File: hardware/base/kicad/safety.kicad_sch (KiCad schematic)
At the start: 14 parts, among them J18 ESTOP, U34 LTV-357T-C, U35 TPS3828-33DBVR

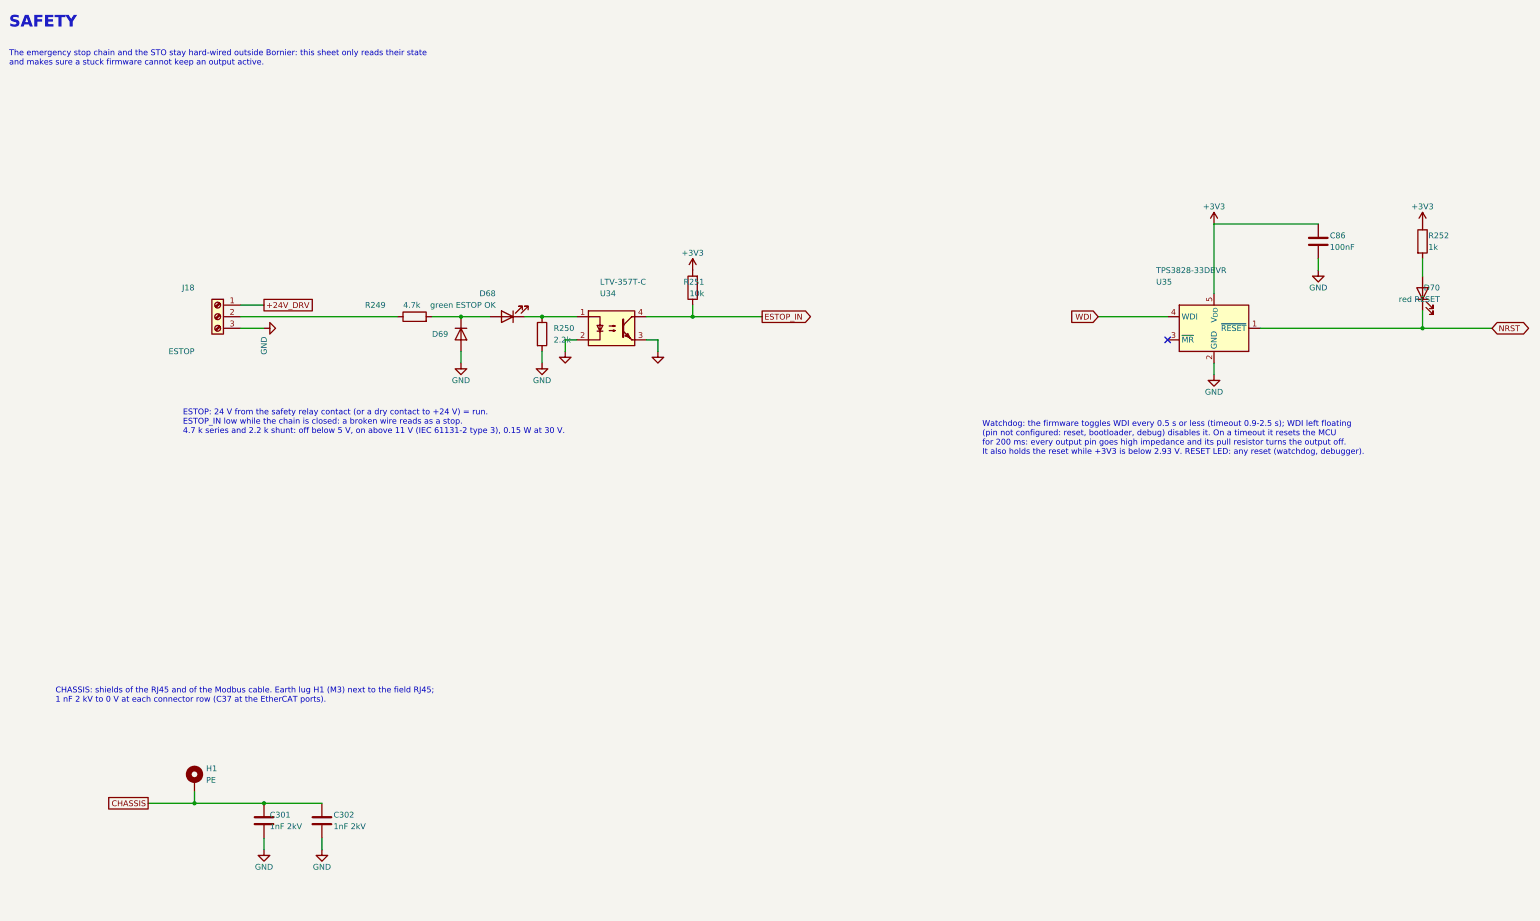
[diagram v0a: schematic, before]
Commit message: Harden the base board protections and unify its terminal blocks
- TVS (SMBJ33CA) on the spindle EN and DIR drains: a relay coil driven
  without a flyback diode no longer avalanches the FET.
- ESD (5 x TPD4E05U06) on every signal of the local bus header.
- A single terminal block type, KF2EDGR-3.81-4P, five times. Pinout rule:
  pole 1 withstands 24 V, pole 2 is 0 V, so the power plug damages
  nothing whichever header it lands in.
- Functional earth on pole 3 of the power terminal block, replacing the
  M3 earth lug.
- 100 k pull-down on the DAC node: the 0-10 V output stays at 0 V while
  the DAC pin is not configured (reset, bootloader).
- "24V OUT" LED on +24V_DRV and test points on the four rails.
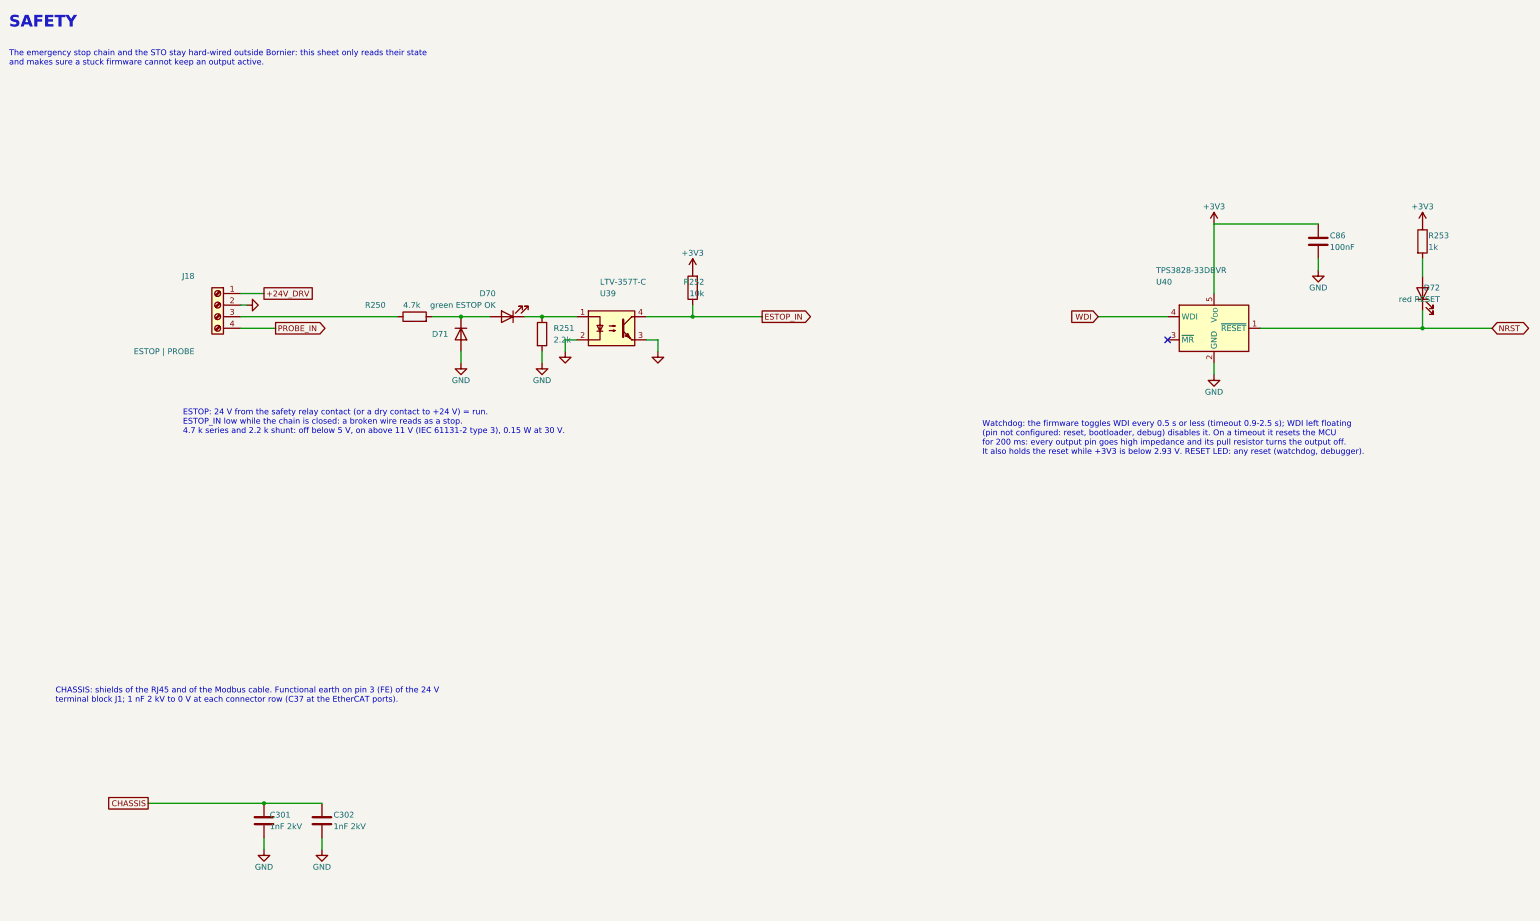
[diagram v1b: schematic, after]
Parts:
- removed D68: green ESTOP OK, LED_SMD:LED_0603_1608Metric, symbol Device:LED
- removed D69: 1N4148WS, Diode_SMD:D_SOD-323, symbol Device:D
- removed H1: PE, MountingHole:MountingHole_3.2mm_M3_Pad_Via, symbol Mechanical:MountingHole_Pad
- removed R249: 4.7k, Resistor_SMD:R_1206_3216Metric, symbol Device:R
- removed U34: LTV-357T-C, Package_SO:SO-4_4.4x3.6mm_P2.54mm, symbol Isolator:LTV-357T
- removed U35: TPS3828-33DBVR, Package_TO_SOT_SMD:SOT-23-5, symbol Power_Supervisor:TPS3823-xxDBV
- added D71: 1N4148WS, Diode_SMD:D_SOD-323, symbol Device:D
- added D72: red RESET, LED_SMD:LED_0603_1608Metric, symbol Device:LED
- added R253: 1k, Resistor_SMD:R_0402_1005Metric, symbol Device:R
- added U39: LTV-357T-C, Package_SO:SO-4_4.4x3.6mm_P2.54mm, symbol Isolator:LTV-357T
- added U40: TPS3828-33DBVR, Package_TO_SOT_SMD:SOT-23-5, symbol Power_Supervisor:TPS3823-xxDBV
- D70: value red RESET -> green ESTOP OK; LCSC C2286 -> C2289
- J18: value ESTOP -> ESTOP | PROBE; footprint Connector_Phoenix_MC:PhoenixContact_MC_1,5_3-G-3.81_1x03_P3.81mm_Horizontal -> Connector_Phoenix_MC:PhoenixContact_MC_1,5_4-G-3.81_1x04_P3.81mm_Horizontal; symbol Connector:Screw_Terminal_01x03 -> Connector:Screw_Terminal_01x04; LCSC C441183 -> C441184
- R250: value 2.2k -> 4.7k; footprint Resistor_SMD:R_0402_1005Metric -> Resistor_SMD:R_1206_3216Metric; LCSC C25879 -> C17936
- R251: value 10k -> 2.2k; LCSC C25744 -> C25879
- R252: value 1k -> 10k; LCSC C11702 -> C25744
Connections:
- net +3V3: now also R252.2, R253.1, U40.5 (V_{DD}); no longer R251.2, R252.1
- net ESTOP_IN: now also R252.1, U39.4; no longer R251.1
- net GND: now also J18.2 (Pin_2), R251.2, D71.2 (A), U39.2, U39.3, U40.2 (GND); no longer J18.3 (Pin_3), R250.2
- net NRST: now also D72.1 (K), U40.1 (~{RESET}); no longer D70.1 (K)
- net WDI: now also U40.4 (WDI)
- net at D70.2 (A): now also R250.2, D71.1 (K); no longer R252.2
- net at R250.1: now also J18.3 (Pin_3)
- new net: D70.1 (K), R251.1, U39.1
- new net: D72.2 (A), R253.2
- new net PROBE_IN: J18.4 (Pin_4)
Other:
- note added: "CHASSIS: shields of the RJ45 and of the Modbus cable. Functional earth on pin 3 (FE) of the 24 V terminal block J1; 1 nF 2 kV to 0 V at each connector row (C37 at the EtherCAT ports)."
- note removed: "CHASSIS: shields of the RJ45 and of the Modbus cable. Earth lug H1 (M3) next to the field RJ45; 1 nF 2 kV to 0 V at each connector row (C37 at the EtherCAT ports)."
- moved on the sheet: D70, R250, R251, R252

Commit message: Accept a 12 V or 24 V supply on the base board (10.8 to 30 V)
- Supply nets renamed +VIN and +VIN_OUT (silkscreen VIN OUT).
- UVLO 200 k over 47 k // 100 k: start 8.47 V (9.48 V worst case),
  stop 7.79 V; fuse 3.5 A (12H1350C).
- 0-10 V: OPA2990 rail-to-rail op amp supplied by +VIN, SS8550 current
  limit across the 120 ohm; 10 V into 10 k from 10.9 V of supply.
- E-stop and probe inputs: 2 x 4.7 k in parallel, shunts 1 k and 4.7 k.
- Buck simulated from 7.8 to 30 V with the smallest slope compensation
  the datasheet allows: 79 deg, 11.6 dB minimum.
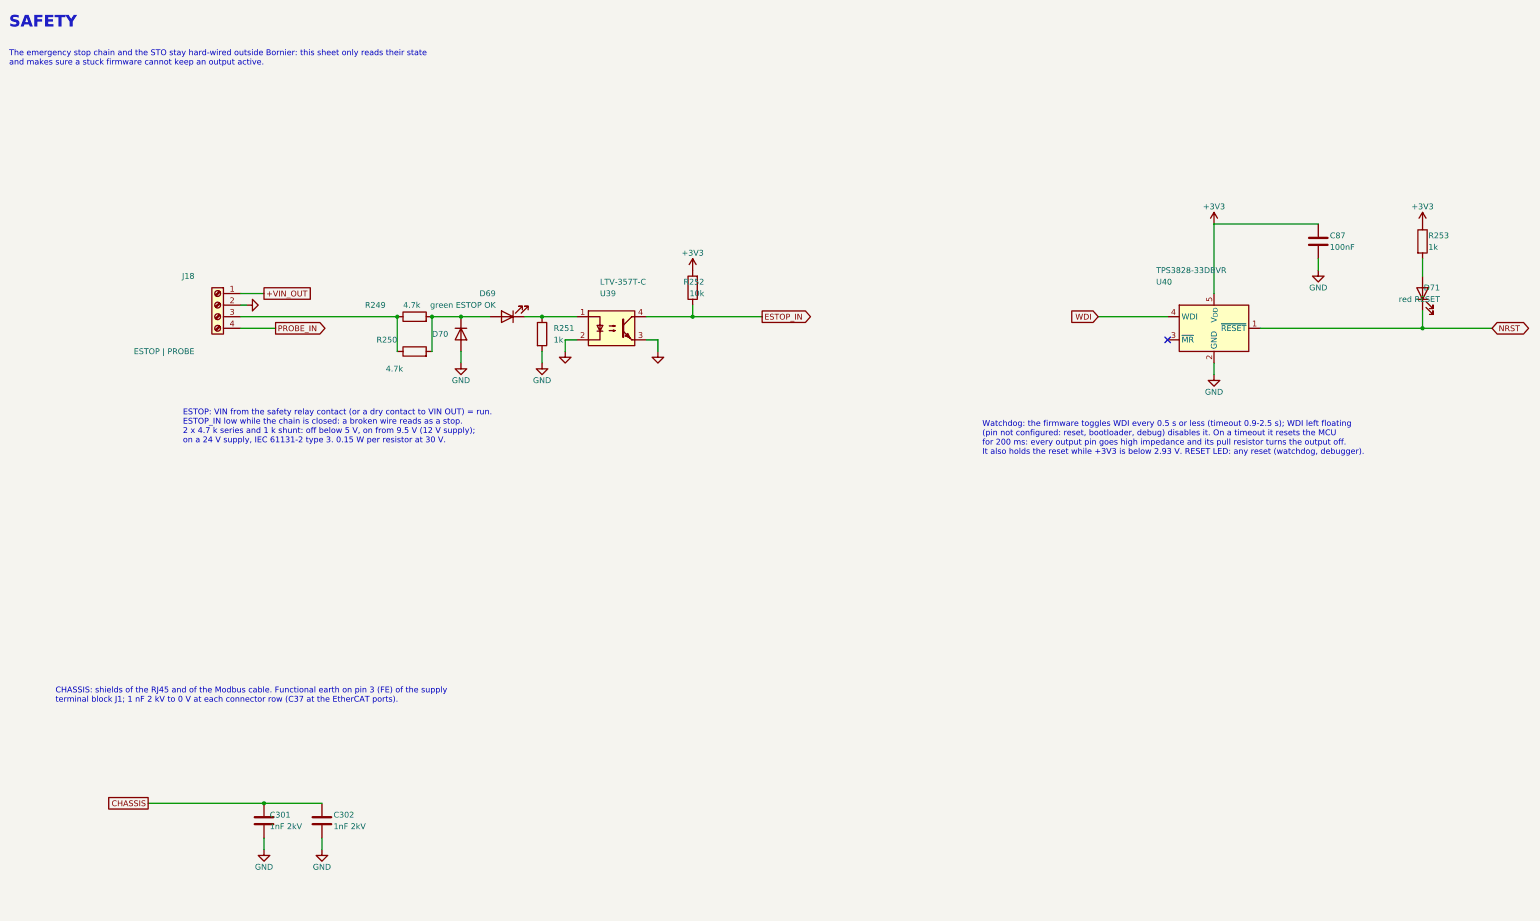
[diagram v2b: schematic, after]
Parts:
- removed C86: 100nF, Capacitor_SMD:C_0402_1005Metric, symbol Device:C
- removed D72: red RESET, LED_SMD:LED_0603_1608Metric, symbol Device:LED
- added C87: 100nF, Capacitor_SMD:C_0402_1005Metric, symbol Device:C
- added D69: green ESTOP OK, LED_SMD:LED_0603_1608Metric, symbol Device:LED
- added R249: 4.7k, Resistor_SMD:R_1206_3216Metric, symbol Device:R
- D70: value green ESTOP OK -> 1N4148WS; footprint LED_SMD:LED_0603_1608Metric -> Diode_SMD:D_SOD-323; symbol Device:LED -> Device:D; LCSC C2289 -> C2128
- D71: value 1N4148WS -> red RESET; footprint Diode_SMD:D_SOD-323 -> LED_SMD:LED_0603_1608Metric; symbol Device:D -> Device:LED; LCSC C2128 -> C2286
- R251: value 2.2k -> 1k; LCSC C25879 -> C11702
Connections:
- net +3V3: now also C87.1
- net GND: now also D70.2 (A), C87.2; no longer D71.2 (A)
- net NRST: now also D71.1 (K)
- net at R251.1, U39.1: now also D69.1 (K); no longer D70.1 (K)
- net at R253.2: now also D71.2 (A)
- net at J18.3 (Pin_3), R250.1: now also R249.1
- net +24V_DRV renamed +VIN_OUT
- new net: D69.2 (A), D70.1 (K), R249.2, R250.2
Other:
- note added: "CHASSIS: shields of the RJ45 and of the Modbus cable. Functional earth on pin 3 (FE) of the supply terminal block J1; 1 nF 2 kV to 0 V at each connector row (C37 at the EtherCAT ports)."
- note added: "ESTOP: VIN from the safety relay contact (or a dry contact to VIN OUT) = run. ESTOP_IN low while the chain is closed: a broken wire reads as a stop. 2 x 4.7 k series and 1 k shunt: off below 5 V, on from 9.5 V (12 V supply); on a 24 V supply, IEC 61131-2 type 3. 0.15 W per resistor at 30 V."
- note removed: "CHASSIS: shields of the RJ45 and of the Modbus cable. Functional earth on pin 3 (FE) of the 24 V terminal block J1; 1 nF 2 kV to 0 V at each connector row (C37 at the EtherCAT ports)."
- note removed: "ESTOP: 24 V from the safety relay contact (or a dry contact to +24 V) = run. ESTOP_IN low while the chain is closed: a broken wire reads as a stop. 4.7 k series and 2.2 k shunt: off below 5 V, on above 11 V (IEC 61131-2 type 3), 0.15 W at 30 V."
- moved on the sheet: R250

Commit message: Add four M3 mounting holes, one plated on CHASSIS
Screw mounting on standoffs for users who do not want the DIN rail profile. H1 is plated and earths CHASSIS through its screw to the panel; the holes stay clear of the profile grooves along the long edges.
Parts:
- added H1: M3 CHASSIS, MountingHole:MountingHole_3.2mm_M3_Pad_Via, symbol Mechanical:MountingHole_Pad
- added H2, H3, H4: M3, MountingHole:MountingHole_3.2mm_M3, symbol Mechanical:MountingHole
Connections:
- net CHASSIS: now also H1.1
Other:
- note added: "H1-H4: M3 holes at the corners, for screws and standoffs on a panel instead of the DIN rail profile; clear of the profile grooves along the long edges. H1 is plated: the screw earths CHASSIS to the panel. Place it at the corner nearest to J1."

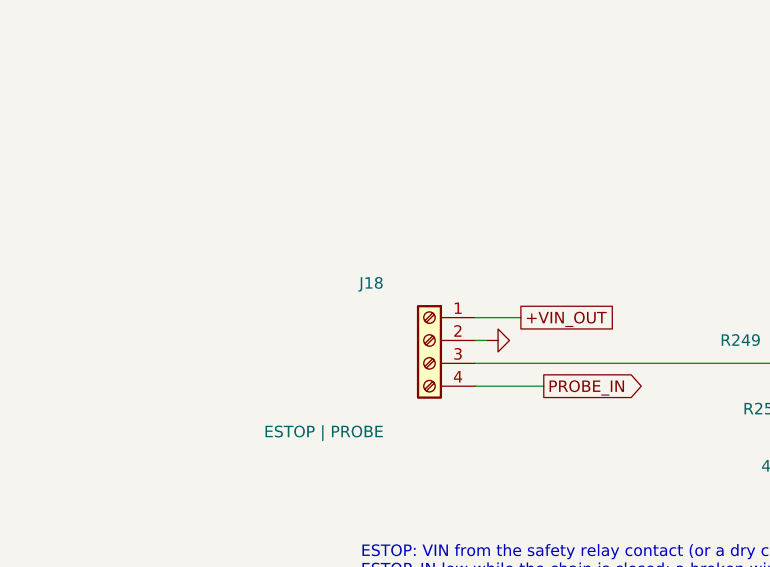
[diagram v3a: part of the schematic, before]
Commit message: Start the base board PCB: outline, profile rules, connectors on the edges
- pcb.py builds the board from the schematic: 72 x 150 mm, 4 layers,
  C-LOCK keyhole, M3 holes, connectors on both long edges; the other
  parts are parked beside the board until they are placed.
- base.kicad_dru: rules of the Phoenix UM-BASIC 72 profile (no part at
  the short edges on the top side, no through-hole lead on the rim the
  board rests on), proved by the DRC.
- Dual shielded RJ45 per axis (HC-WK88-H132-1X2-55B): port A for the
  drive, port B for the encoder. kicadgen draws multi-unit symbols, one
  unit per sheet; footprint and 3D model generated from the datasheet.
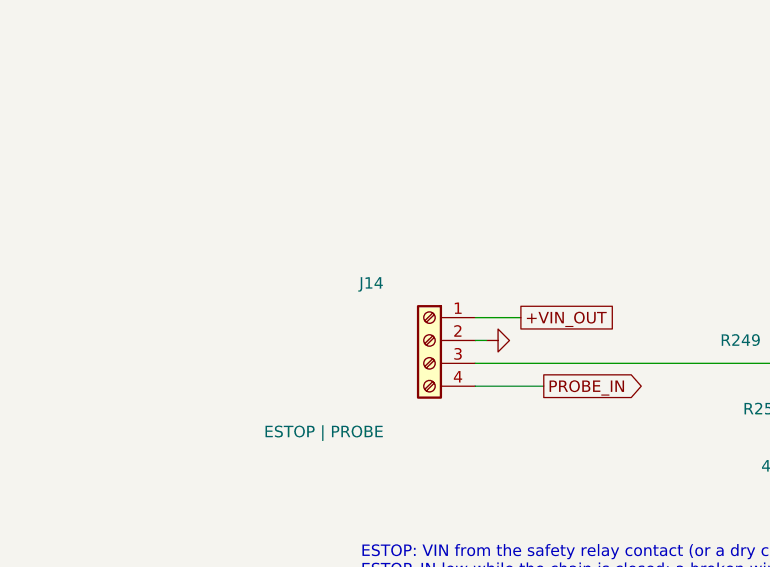
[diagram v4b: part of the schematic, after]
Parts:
- removed J18: ESTOP | PROBE, Connector_Phoenix_MC:PhoenixContact_MC_1,5_4-G-3.81_1x04_P3.81mm_Horizontal, symbol Connector:Screw_Terminal_01x04
- added J14: ESTOP | PROBE, Connector_Phoenix_MC:PhoenixContact_MC_1,5_4-G-3.81_1x04_P3.81mm_Horizontal, symbol Connector:Screw_Terminal_01x04
- H1: footprint MountingHole:MountingHole_3.2mm_M3_Pad_Via -> MountingHole:MountingHole_3.2mm_M3_Pad
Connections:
- net +VIN_OUT: now also J14.1 (Pin_1)
- net GND: now also J14.2 (Pin_2)
- net PROBE_IN: now also J14.4 (Pin_4)
- net at R249.1, R250.1: now also J14.3 (Pin_3)

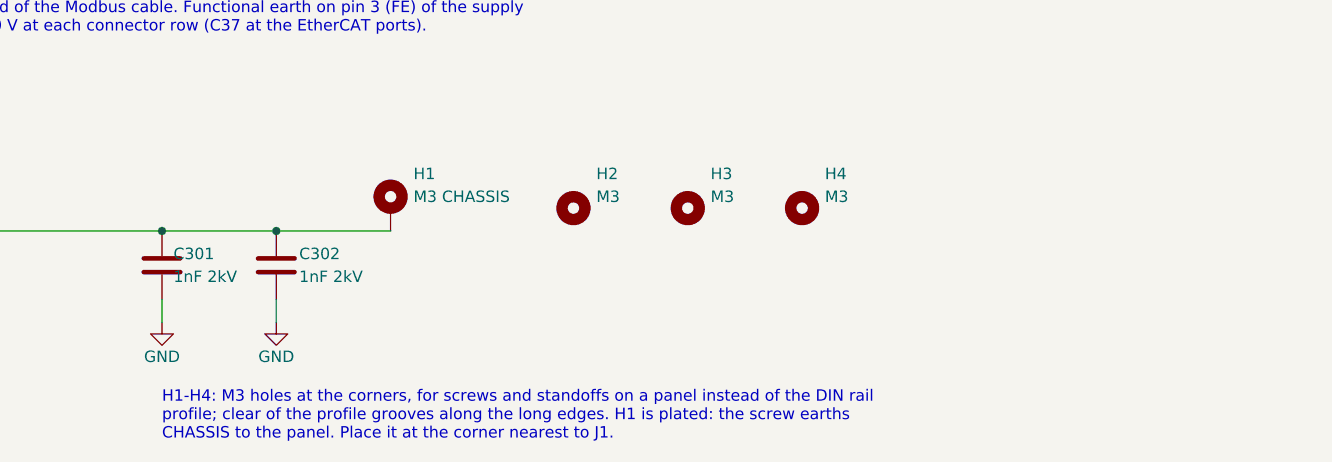
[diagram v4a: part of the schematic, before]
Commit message: Widen the base board to 107.5 x 150 mm, vertical USB, PE contact hole
- The parts covered 94 % of the free top area on 72 mm, 53 % on 107.5 mm:
  Phoenix UM-BASIC 108 profile (kit UM-BASIC-KIT-B108-L150-7035), one side.
- M3 holes at the four corners; H1 plated next to POWER.
- H5: plated hole for the Phoenix PE contact L1, which earths CHASSIS to
  the DIN rail; no lead over the contact body under the board.
- USB jack: vertical Molex 105133-0001, to sit next to the MCU.
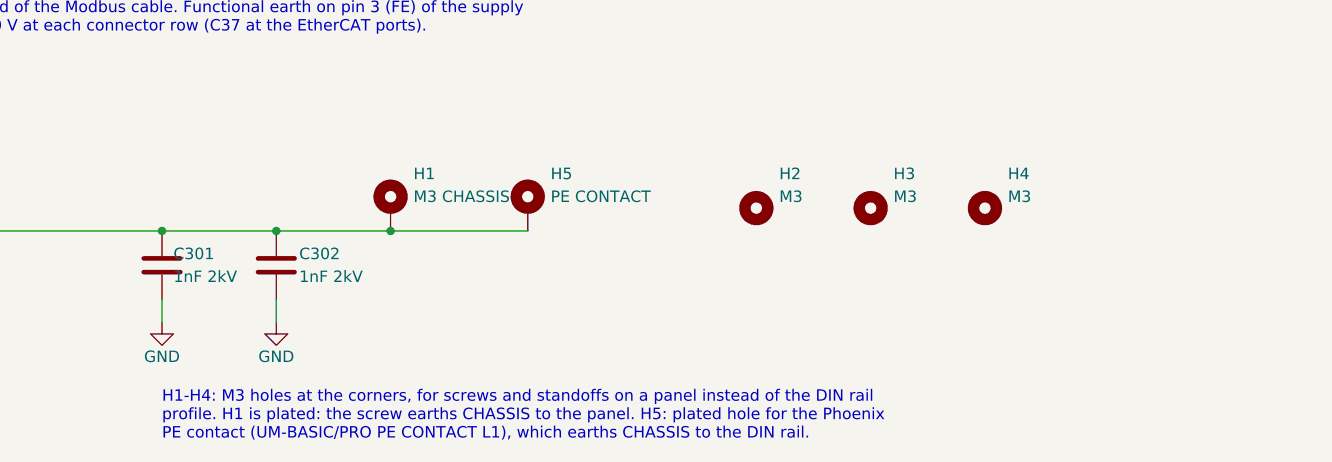
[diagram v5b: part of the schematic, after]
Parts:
- added H5: PE CONTACT, MountingHole:MountingHole_3.2mm_M3_Pad, symbol Mechanical:MountingHole_Pad
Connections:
- net CHASSIS: now also H5.1
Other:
- note added: "H1-H4: M3 holes at the corners, for screws and standoffs on a panel instead of the DIN rail profile. H1 is plated: the screw earths CHASSIS to the panel. H5: plated hole for the Phoenix PE contact (UM-BASIC/PRO PE CONTACT L1), which earths CHASSIS to the DIN rail."
- note removed: "H1-H4: M3 holes at the corners, for screws and standoffs on a panel instead of the DIN rail profile; clear of the profile grooves along the long edges. H1 is plated: the screw earths CHASSIS to the panel. Place it at the corner nearest to J1."
- moved on the sheet: H2, H3, H4
